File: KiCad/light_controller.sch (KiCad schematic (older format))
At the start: 24 parts

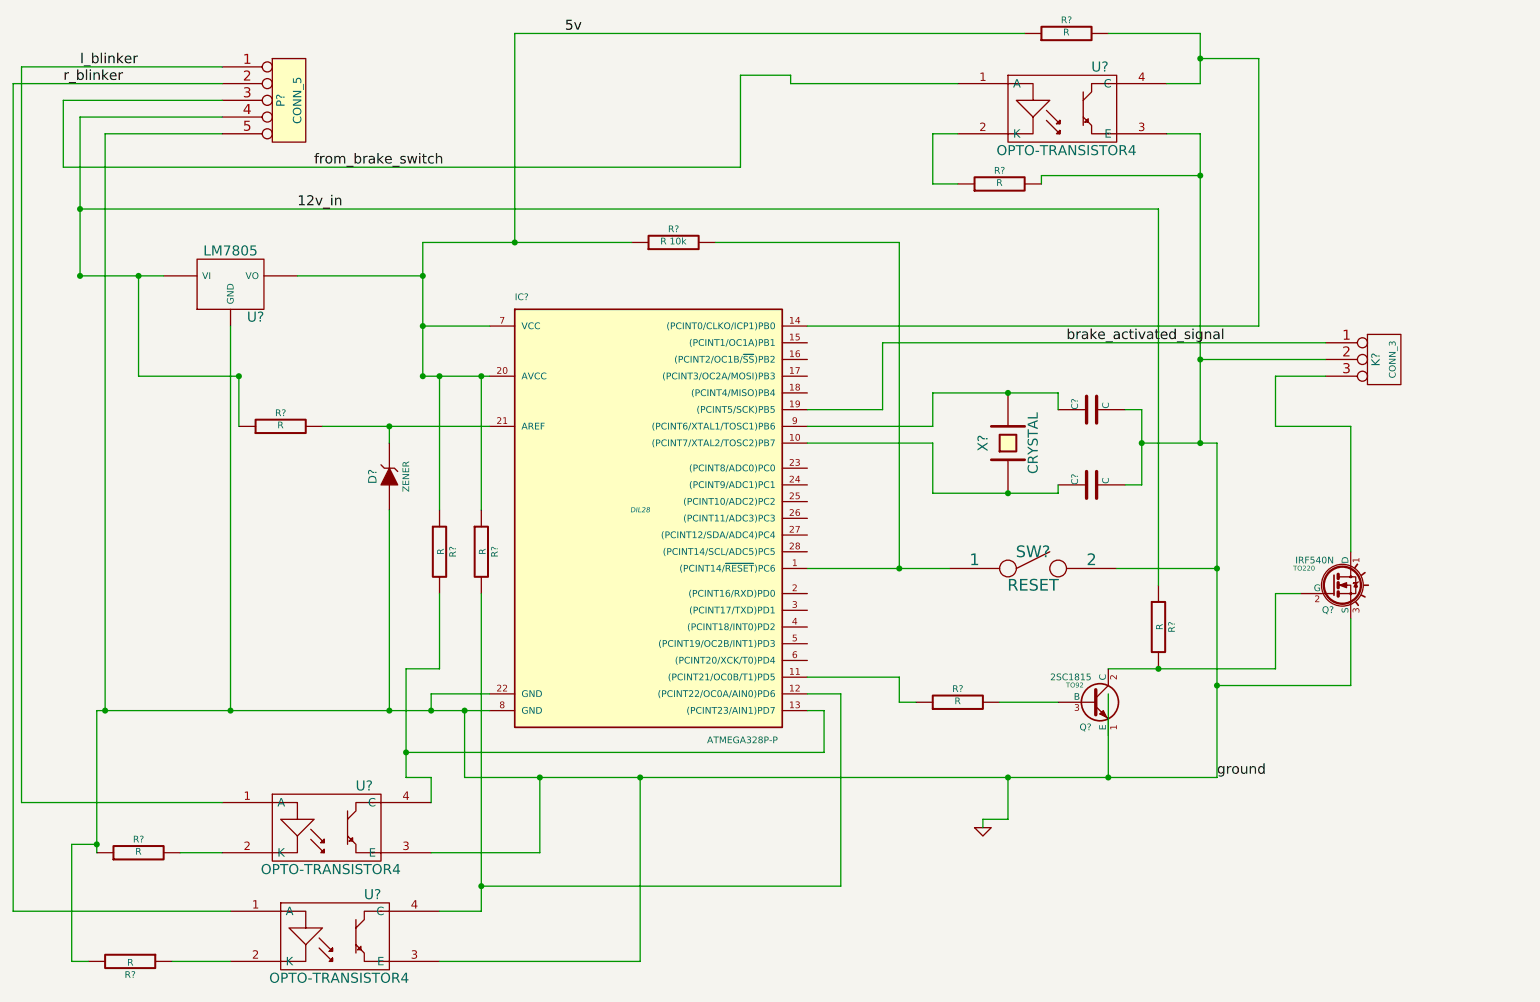
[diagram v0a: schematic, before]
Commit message: Schematic updates
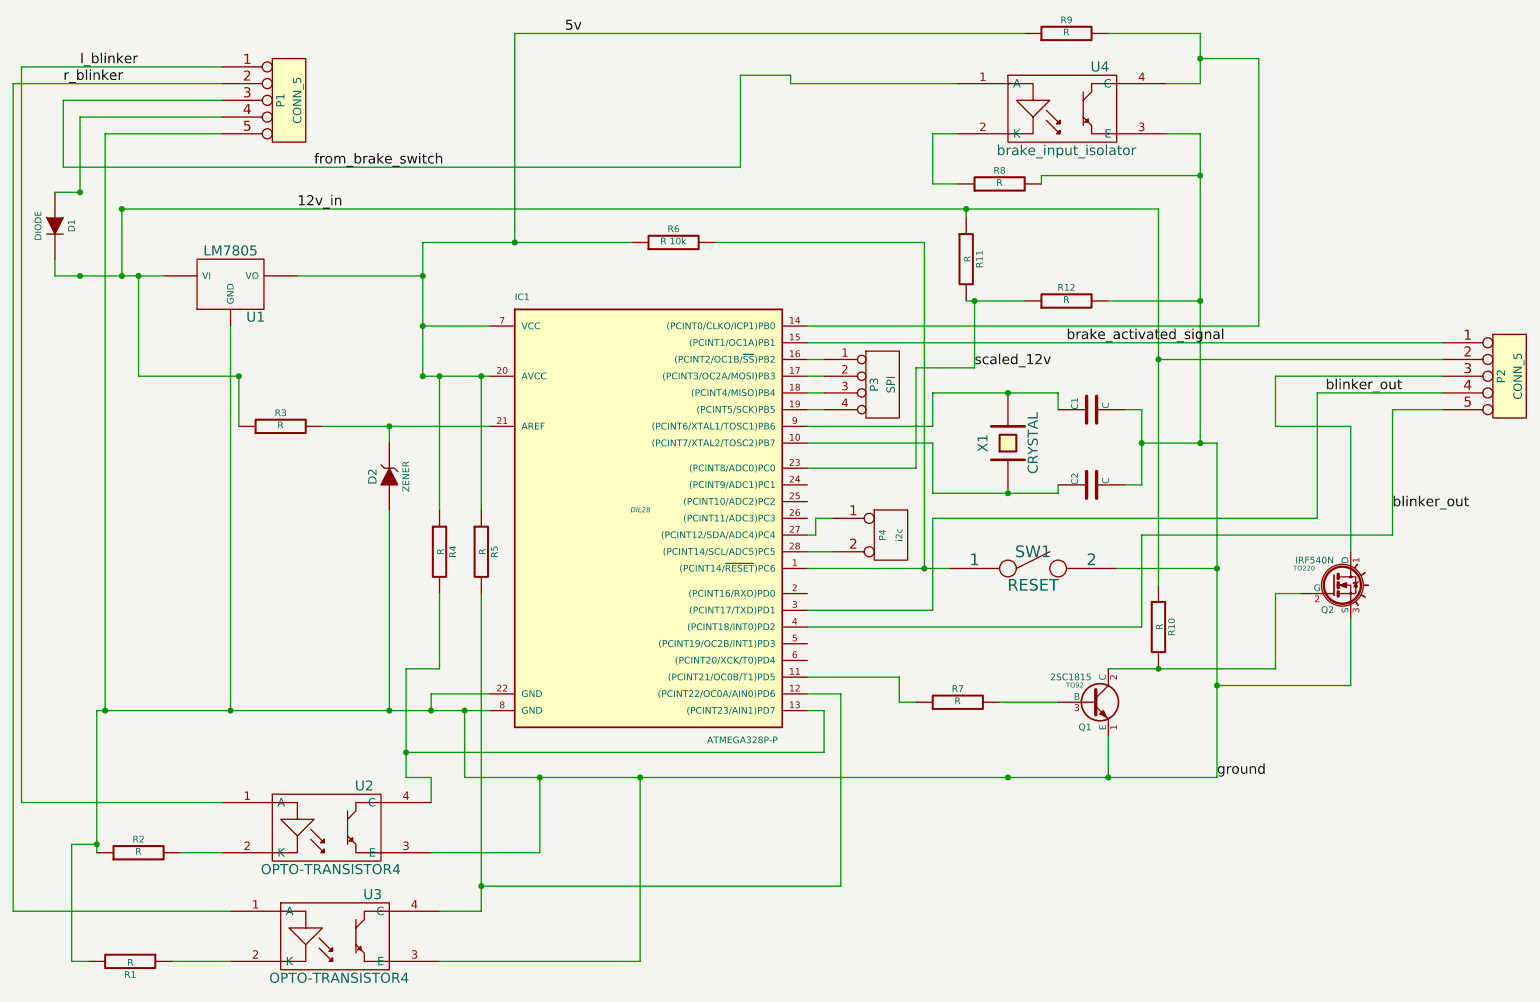
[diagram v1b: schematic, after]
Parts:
- removed K?: CONN_3, symbol CONN_3
- added D1: DIODE, ~, symbol DIODE
- added P2: CONN_5, symbol CONN_5
- added P3: SPI, symbol CONN_4
- added P4: i2c, symbol CONN_2
- added R11, R12: R, ~, symbol R
- U4: renamed from U?; value OPTO-TRANSISTOR4 -> brake_input_isolator
- gave numbers to parts that had none: 22
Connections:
- net GND is gone; now on net ground: C1.2, C2.2, D2.1 (A), IC1.22 (GND), IC1.8 (GND), P1.5, Q2.3 (S), R1.2, R2.1, R8.2, SW1.2, U1.GND, U2.3 (E), U3.3 (E), U4.3 (E)
- net 12v_in: now also D1.2 (K), P2.2, R11.1; no longer P1.4
- net brake_activated_signal: now also IC1.15 ((PCINT1/OC1A)PB1), P2.1; no longer IC1.19 ((PCINT5/SCK)PB5)
- net at IC1.16 ((PCINT2/OC1B/~SS~)PB2): now also P3.1 (P1)
- net at IC1.17 ((PCINT3/OC2A/MOSI)PB3): now also P3.2 (P2)
- net at IC1.18 ((PCINT4/MISO)PB4): now also P3.3 (P3)
- net scaled_12v: now reaches IC1.23 ((PCINT8/ADC0)PC0)
- net scaled_12v: now also R11.2, R12.1
- net at IC1.27 ((PCINT12/SDA/ADC4)PC4): now also P4.1 (P1)
- net at IC1.28 ((PCINT14/SCL/ADC5)PC5): now also P4.2 (PM)
- net blinker_out: now reaches IC1.3 ((PCINT17/TXD)PD1)
- net blinker_out: now also IC1.4 ((PCINT18/INT0)PD2), P2.4, P2.5
- net at Q2.1 (D): now also P2.3
- net ground: now reaches Q1.1 (E)
- net ground: now also R12.2
- new net: IC1.19 ((PCINT5/SCK)PB5), P3.4 (P4)
- new net: D1.1 (A), P1.4
